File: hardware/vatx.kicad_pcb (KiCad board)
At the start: 2 copper layers, 50 x 50.1 mm, 27 parts, among them J1 USB, P1 CONN_10X2, P3 CONN_1, P4 CONN_1, P5 CONN_1, P6 CONN_1, P7 CONN_1, SW1 SWITCH_INV, U1 LM317T

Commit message: scheme/pcb version again via for heatsink
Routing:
- net +VAR: track 38.4 -> 55.5 mm, vias 5 -> 9
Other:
- board text added: "v2.0"

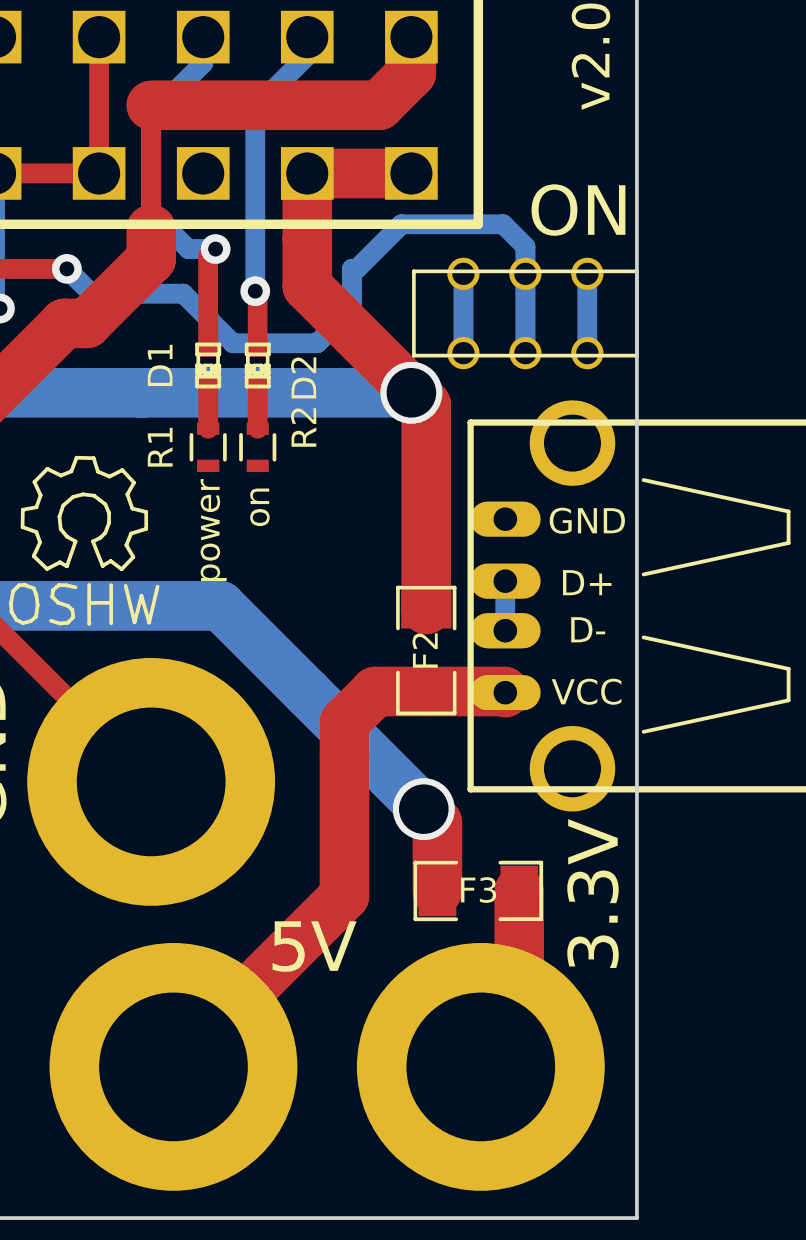
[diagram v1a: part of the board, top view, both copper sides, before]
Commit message: Add power resistor some PSU need that to deliver current
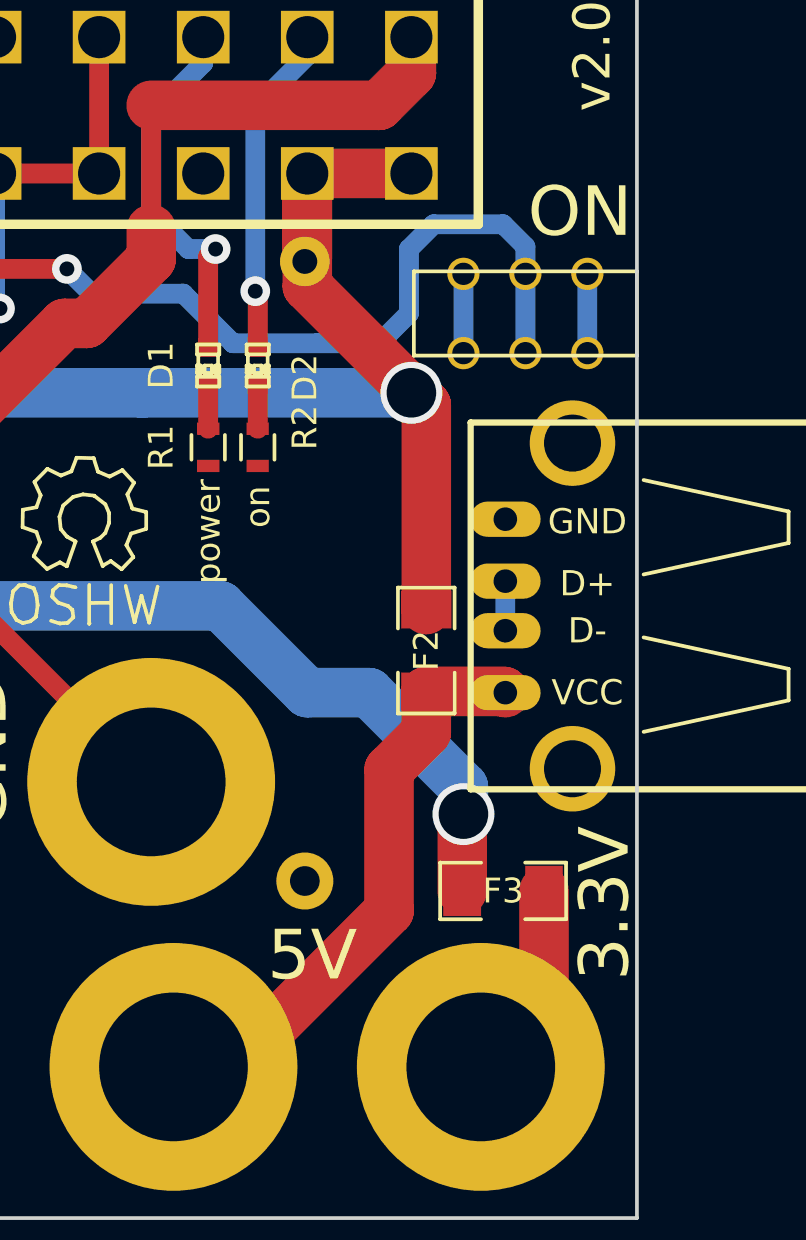
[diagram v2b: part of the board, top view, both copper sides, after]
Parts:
- added R5: 10 9W, Resistors_ThroughHole:Resistor_Horizontal_RM25mm, B.Cu at (143.4, 73.6)
- moved F3 1.00 mm to (151.4, 86.5)
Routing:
- net +5V: track 68.0 -> 71.6 mm
- net f+3.3V: track 7.74 -> 10.4 mm
- net +3.3V: track 63.8 -> 65.7 mm
- net PSON: track 41.1 -> 41.7 mm
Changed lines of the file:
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@@
 (kicad_pcb (version 4) (host pcbnew "(2014-09-02 BZR 5112)-product")
   (general
-    (links 51)
+    (links 53)
     (no_connects 0)
     (area 91.223919 33.15 180.933333 101.525)
     (thickness 1.6)
     (drawings 22)
-    (tracks 172)
+    (tracks 177)
     (zones 0)
-    (modules 27)
+    (modules 28)
     (nets 22)
   )
@@
   )
   (module SMD_Packages:SMD-1206 (layer F.Cu)
-    (at 150.4 86.5)
+    (at 151.4 86.5)
     (attr smd)
     (fp_text reference F3 (at 0 0) (layer F.SilkS)
@@
     (pad SG2 thru_hole circle (at 6.57 0 90) (size 3.45 3.45) (drill 2.3) (layers *.Cu *.Mask))
   )
+  (module Resistors_ThroughHole:Resistor_Horizontal_RM25mm (layer B.Cu)
+    (at 143.4 73.6 270)
+    (descr "Resistor, Axial, RM 25mm,")
+    (tags "Resistor, Axial, RM 25mm,")
+    (fp_text reference R5 (at 0 5.75056 270) (layer B.SilkS)
+      (effects (font (size 1 1) (thickness 0.15)) (justify mirror))
+    )
+    (fp_text value "10 9W" (at 0 -6.49986 270) (layer B.SilkS) hide
+      (effects (font (size 1 1) (thickness 0.15)) (justify mirror))
+    )
+    (fp_line (start -8.94334 0) (end -10.97534 0) (layer B.SilkS) (width 0.15))
+    (fp_line (start 9.34466 0) (end 10.86866 0) (layer B.SilkS) (width 0.15))
+    (fp_line (start -8.68934 3.81) (end -8.68934 -3.81) (layer B.SilkS) (width 0.15))
+    (fp_line (start -8.68934 -3.81) (end 9.09066 -3.81) (layer B.SilkS) (width 0.15))
+    (fp_line (start 9.09066 -3.81) (end 9.09066 3.81) (layer B.SilkS) (width 0.15))
+    (fp_line (start 9.09066 3.81) (end -8.68934 3.81) (layer B.SilkS) (width 0.15))
+    (pad 1 thru_hole circle (at -12.49934 0 270) (size 1.99898 1.99898) (drill 1.00076) (layers *.Cu *.SilkS *.Mask)
+      (net 8 +5V))
+    (pad 2 thru_hole circle (at 12.49934 0 270) (size 2.30124 2.30124) (drill 1.19888) (layers *.Cu *.SilkS *.Mask)
+      (net 10 GND))
+  )
   (gr_text v2.0 (at 155 52.8 90) (layer F.SilkS)
     (effects (font (size 1.5 1.5) (thickness 0.3)))
@@
     (effects (font (size 2 2) (thickness 0.3)))
   )
-  (gr_text 5V (at 143.7 88.8) (layer F.SilkS)
+  (gr_text 5V (at 143.7 89.1) (layer F.SilkS)
     (effects (font (size 2 2) (thickness 0.3)))
   )
-  (gr_text 3.3V (at 155.1 86.7 90) (layer F.SilkS)
+  (gr_text 3.3V (at 155.5 87 90) (layer F.SilkS)
     (effects (font (size 2 2) (thickness 0.3)))
   )
@@
   (segment (start 128.2 70.275) (end 128.2 69.1) (width 2) (layer F.Cu) (net 5))
   (segment (start 137.2 54.8) (end 146.4 54.8) (width 2) (layer F.Cu) (net 5))
-  (segment (start 123.8 63.925) (end 121.025 63.925) (width 0.8) (layer F.Cu) (net 6) (status 400000))
+  (segment (start 123.8 63.925) (end 121.025 63.925) (width 0.8) (layer F.Cu) (net 6))
   (via (at 117.5 60.7) (size 1.2) (layers F.Cu B.Cu) (net 6))
   (segment (start 119.4 60.7) (end 117.5 60.7) (width 0.8) (layer F.Cu) (net 6))
@@
   (via (at 121 63.9) (size 1.2) (layers F.Cu B.Cu) (net 6))
   (segment (start 121.025 63.925) (end 121 63.9) (width 0.8) (layer F.Cu) (net 6))
-  (segment (start 123.8 63.925) (end 123.725 63.925) (width 0.8) (layer F.Cu) (net 6) (status C00000))
+  (segment (start 123.8 63.925) (end 123.725 63.925) (width 0.8) (layer F.Cu) (net 6))
   (segment (start 123.8 63.925) (end 127.4225 63.925) (width 0.8) (layer F.Cu) (net 6))
   (segment (start 127.4225 63.925) (end 127.6475 63.7) (width 0.8) (layer F.Cu) (net 6))
@@
   (segment (start 148.2 66.9) (end 148.3 66.9) (width 2) (layer F.Cu) (net 8))
   (segment (start 136.8 66.4) (end 147.7 66.4) (width 2) (layer B.Cu) (net 8))
+  (segment (start 143.49898 61.00168) (end 143.4 61.10066) (width 2) (layer F.Cu) (net 8))
+  (segment (start 143.49898 57.55082) (end 143.49898 61.00168) (width 2) (layer F.Cu) (net 8))
   (segment (start 151.49 74) (end 151.49 76) (width 0.8) (layer B.Cu) (net 9))
   (segment (start 130.90058 57.55082) (end 135.0992 57.55082) (width 0.8) (layer F.Cu) (net 10))
@@
   (segment (start 109.89986 52.04918) (end 109.89986 57.55082) (width 2) (layer F.Cu) (net 11))
   (segment (start 114.10102 52.04918) (end 109.89986 52.04918) (width 2) (layer F.Cu) (net 11))
-  (via (at 148.2 83.2) (size 2.5) (drill 2) (layers F.Cu B.Cu) (net 11))
-  (segment (start 148.2 83.2) (end 148.749 83.749) (width 2) (layer F.Cu) (net 11))
-  (segment (start 148.749 83.749) (end 148.749 86.5) (width 2) (layer F.Cu) (net 11))
+  (segment (start 146 78.5) (end 149.8 82.3) (width 2) (layer B.Cu) (net 11))
+  (segment (start 149.8 82.3) (end 149.8 83.4) (width 2) (layer B.Cu) (net 11))
+  (via (at 149.8 83.4) (size 2.5) (drill 2) (layers F.Cu B.Cu) (net 11))
+  (segment (start 149.8 83.4) (end 149.749 83.451) (width 2) (layer F.Cu) (net 11))
+  (segment (start 149.749 83.451) (end 149.749 86.5) (width 2) (layer F.Cu) (net 11))
+  (segment (start 109.89986 57.55082) (end 109.89986 60.29986) (width 2) (layer B.Cu) (net 11))
+  (segment (start 124.6 75) (end 109.89986 60.29986) (width 2) (layer B.Cu) (net 11))
+  (segment (start 140 75) (end 124.6 75) (width 2) (layer B.Cu) (net 11))
   (segment (start 143.5 78.5) (end 140 75) (width 2) (layer B.Cu) (net 11))
-  (segment (start 140 75) (end 124.6 75) (width 2) (layer B.Cu) (net 11))
-  (segment (start 124.6 75) (end 109.89986 60.29986) (width 2) (layer B.Cu) (net 11))
-  (segment (start 109.89986 57.55082) (end 109.89986 60.29986) (width 2) (layer B.Cu) (net 11))
-  (segment (start 143.5 78.5) (end 148.2 83.2) (width 2) (layer B.Cu) (net 11))
-  (segment (start 145.5 61.4) (end 147.3 59.6) (width 0.8) (layer B.Cu) (net 13))
-  (segment (start 147.3 59.6) (end 151.4 59.6) (width 0.8) (layer B.Cu) (net 13))
+  (segment (start 143.5 78.5) (end 146 78.5) (width 2) (layer B.Cu) (net 11))
+  (segment (start 143.9 64.4) (end 146.4 64.4) (width 0.8) (layer B.Cu) (net 13))
+  (segment (start 122.5008 59.0008) (end 124.9 61.4) (width 0.8) (layer F.Cu) (net 13))
+  (segment (start 124.9 61.4) (end 133.8 61.4) (width 0.8) (layer F.Cu) (net 13))
+  (via (at 133.8 61.4) (size 1.2) (layers F.Cu B.Cu) (net 13))
+  (segment (start 133.8 61.4) (end 134.8 62.4) (width 0.8) (layer B.Cu) (net 13))
+  (segment (start 134.8 62.4) (end 138.5 62.4) (width 0.8) (layer B.Cu) (net 13))
+  (segment (start 138.5 62.4) (end 140.5 64.4) (width 0.8) (layer B.Cu) (net 13))
+  (segment (start 140.5 64.4) (end 143.9 64.4) (width 0.8) (layer B.Cu) (net 13))
+  (segment (start 122.5008 57.55082) (end 122.5008 59.0008) (width 0.8) (layer F.Cu) (net 13))
+  (segment (start 152.3 60.5) (end 152.3 61.6) (width 0.8) (layer B.Cu) (net 13) (status 800000))
   (segment (start 151.4 59.6) (end 152.3 60.5) (width 0.8) (layer B.Cu) (net 13))
-  (segment (start 152.3 60.5) (end 152.3 61.6) (width 0.8) (layer B.Cu) (net 13))
-  (segment (start 122.5008 57.55082) (end 122.5008 59.0008) (width 0.8) (layer F.Cu) (net 13))
-  (segment (start 145.3 63) (end 145.3 61.4) (width 0.8) (layer B.Cu) (net 13))
-  (segment (start 143.9 64.4) (end 145.3 63) (width 0.8) (layer B.Cu) (net 13))
-  (segment (start 140.5 64.4) (end 143.9 64.4) (width 0.8) (layer B.Cu) (net 13))
-  (segment (start 138.5 62.4) (end 140.5 64.4) (width 0.8) (layer B.Cu) (net 13))
-  (segment (start 134.8 62.4) (end 138.5 62.4) (width 0.8) (layer B.Cu) (net 13))
-  (segment (start 133.8 61.4) (end 134.8 62.4) (width 0.8) (layer B.Cu) (net 13))
-  (via (at 133.8 61.4) (size 1.2) (layers F.Cu B.Cu) (net 13))
-  (segment (start 124.9 61.4) (end 133.8 61.4) (width 0.8) (layer F.Cu) (net 13))
-  (segment (start 122.5008 59.0008) (end 124.9 61.4) (width 0.8) (layer F.Cu) (net 13))
-  (segment (start 145.3 61.4) (end 145.5 61.4) (width 0.8) (layer B.Cu) (net 13))
+  (segment (start 148.6 59.6) (end 151.4 59.6) (width 0.8) (layer B.Cu) (net 13))
+  (segment (start 147.6 60.6) (end 148.6 59.6) (width 0.8) (layer B.Cu) (net 13))
+  (segment (start 147.6 63.2) (end 147.6 60.6) (width 0.8) (layer B.Cu) (net 13))
+  (segment (start 146.4 64.4) (end 147.6 63.2) (width 0.8) (layer B.Cu) (net 13))
   (segment (start 152.3 61.6) (end 152.3 64.8) (width 0.8) (layer B.Cu) (net 13))
   (segment (start 116.75 73.25) (end 113.4 76.6) (width 0.8) (layer F.Cu) (net 15))
   (segment (start 113.4 76.6) (end 110.6 76.6) (width 0.8) (layer F.Cu) (net 15))
   (segment (start 118.9 73.25) (end 116.75 73.25) (width 0.8) (layer F.Cu) (net 15))
-  (segment (start 145 79.7) (end 146.249 78.451) (width 2) (layer F.Cu) (net 16))
-  (segment (start 146.249 78.451) (end 148.3 78.451) (width 2) (layer F.Cu) (net 16))
-  (segment (start 145 81) (end 145 86.7) (width 2) (layer F.Cu) (net 16))
-  (segment (start 138.1 93.6) (end 145 86.7) (width 2) (layer F.Cu) (net 16))
-  (segment (start 145 81) (end 145 79.7) (width 2) (layer F.Cu) (net 16))
   (segment (start 151.441 78.451) (end 151.49 78.5) (width 2) (layer F.Cu) (net 16))
   (segment (start 148.3 78.451) (end 151.441 78.451) (width 2) (layer F.Cu) (net 16))
+  (segment (start 140.5 93.6) (end 138.1 93.6) (width 2) (layer F.Cu) (net 16))
+  (segment (start 148.3 80.1) (end 146.8 81.6) (width 2) (layer F.Cu) (net 16))
+  (segment (start 146.8 81.6) (end 146.8 87.3) (width 2) (layer F.Cu) (net 16))
+  (segment (start 146.8 87.3) (end 140.5 93.6) (width 2) (layer F.Cu) (net 16))
+  (segment (start 148.3 78.451) (end 148.3 80.1) (width 2) (layer F.Cu) (net 16))
   (segment (start 152.051 92.049) (end 150.5 93.6) (width 2) (layer F.Cu) (net 17))
-  (segment (start 152.051 86.5) (end 152.051 92.049) (width 2) (layer F.Cu) (net 17))
+  (segment (start 153.051 91.049) (end 150.5 93.6) (width 2) (layer F.Cu) (net 17))
+  (segment (start 153.051 86.5) (end 153.051 91.049) (width 2) (layer F.Cu) (net 17))
   (segment (start 109.8 90.5) (end 112.9 93.6) (width 0.8) (layer F.Cu) (net 18))
   (segment (start 109.8 90.5) (end 112.9 93.6) (width 2) (layer F.Cu) (net 18))

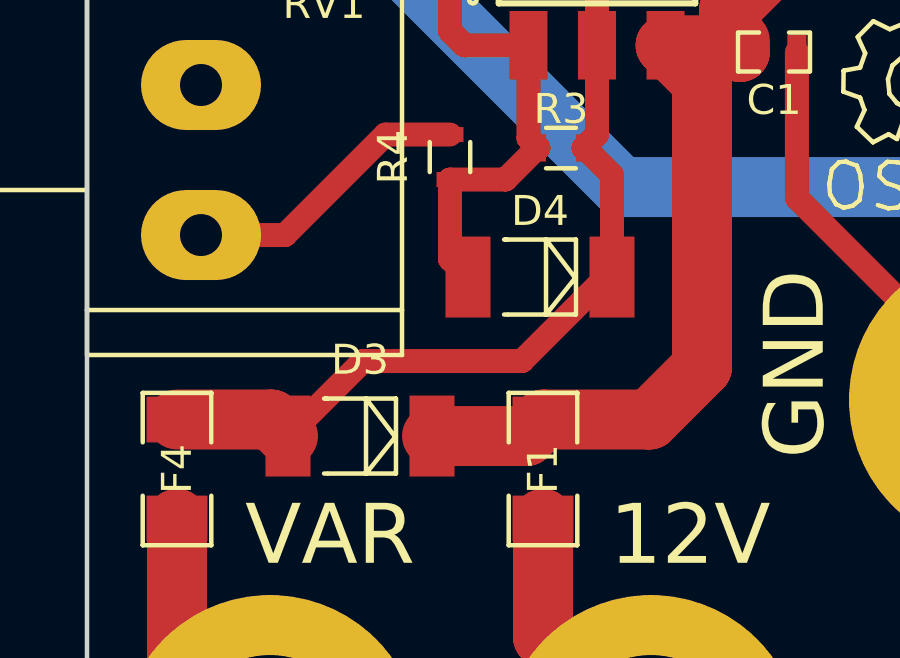
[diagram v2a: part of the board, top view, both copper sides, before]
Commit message: Set seeed opl diode footprint
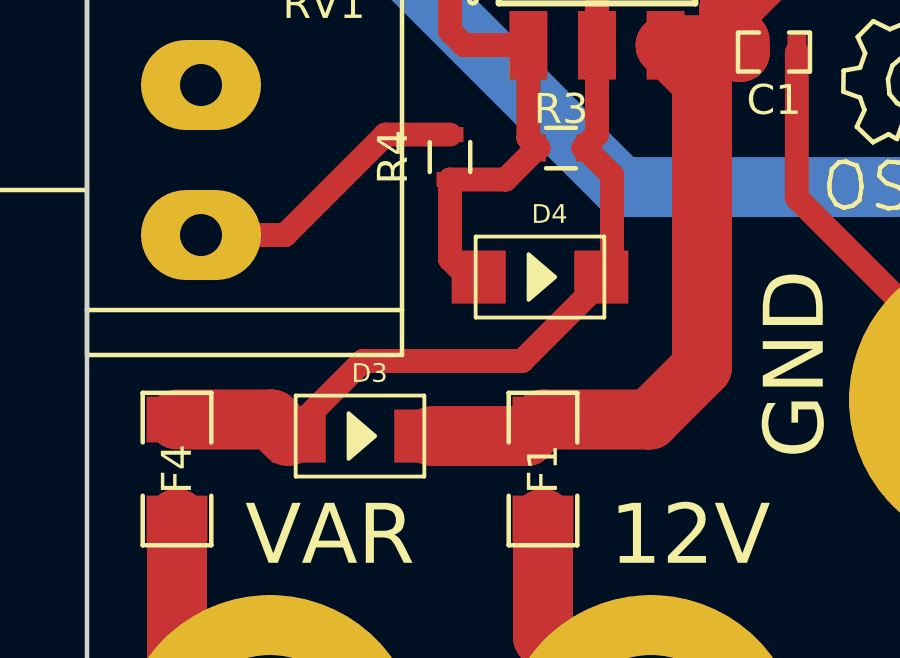
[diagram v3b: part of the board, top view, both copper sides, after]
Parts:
- D3, D4: footprint Diodes_SMD:Diode-MELF_Standard -> opl:DO-214AC

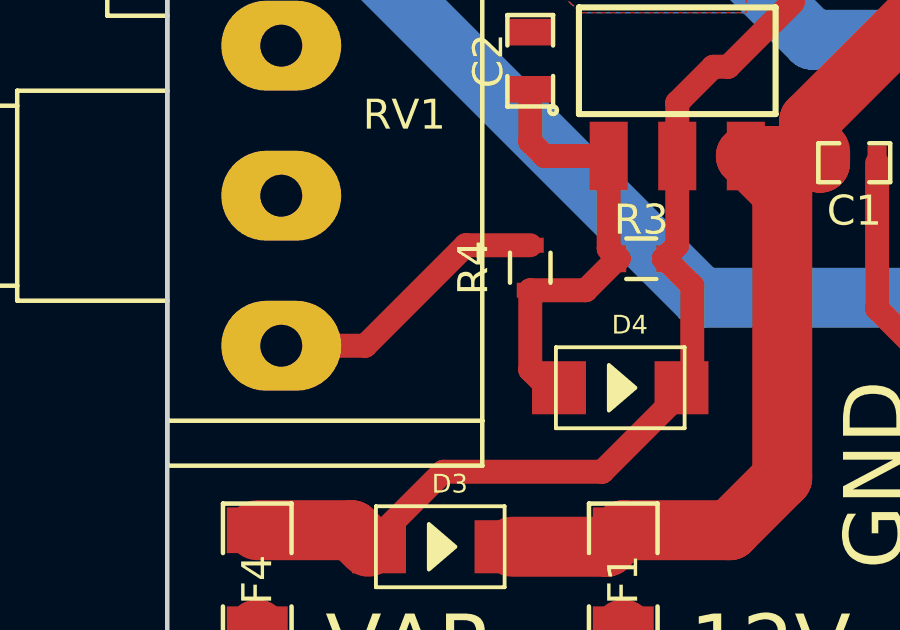
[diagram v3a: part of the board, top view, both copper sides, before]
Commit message: Update +VAR : remove R4 R1/R2 values updated for choosen leds Seeed BOM
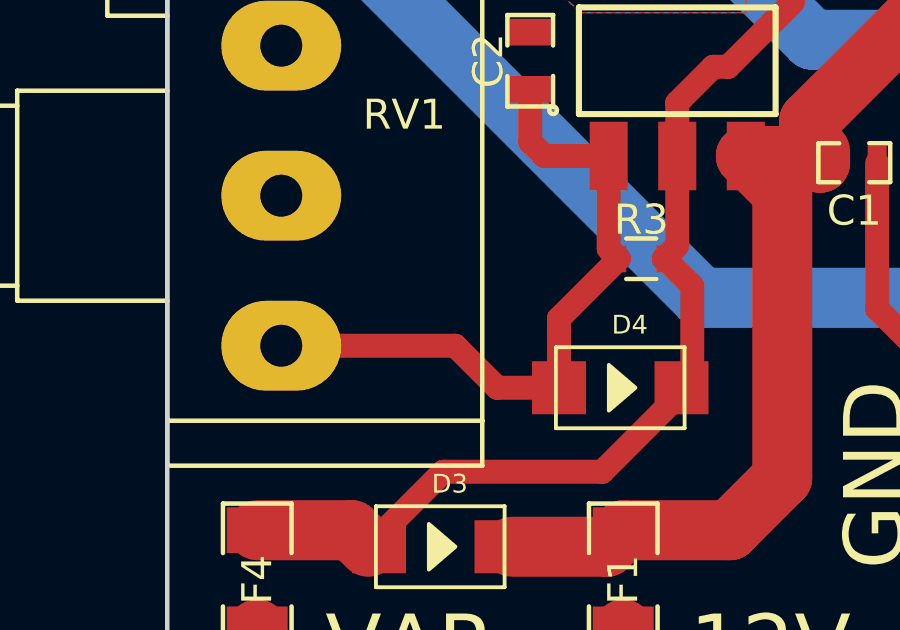
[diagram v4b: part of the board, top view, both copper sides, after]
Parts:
- removed R4: 220, Resistors_SMD:R_0603
- R1: value 330 -> 470
- R2: value 330 -> 680
- R3: value 150 -> 100
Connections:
- RV1 pad 1: Net-(R4-Pad2) -> Net-(C2-Pad1)
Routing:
- net Net-(R4-Pad2): track 9.69 -> 0.00 mm
- net Net-(C2-Pad1): track 15.0 -> 23.1 mm

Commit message: documentation
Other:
- board text added: "vATX v2.0"
- board text removed: "v2.0"
